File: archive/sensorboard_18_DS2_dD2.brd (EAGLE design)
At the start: 100 x 58 mm, 91 parts, among them IC1 ECMF02-2AMX6, IC2_ESP32S2WROOMM22S2 ESP32-S2-WROOM_M22S2H3200PH3Q0, J1_CONN._ADAPTERB. RJ12, J4_USB USB_CONN, J6_OAT 2.5mm JACK, J7_I2C RJ12, U1 LPS22HB, U10-MAG_SENSOR MMC5983MA, U11 LDL212PV33R, U12 NCV8163ASN330T1G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

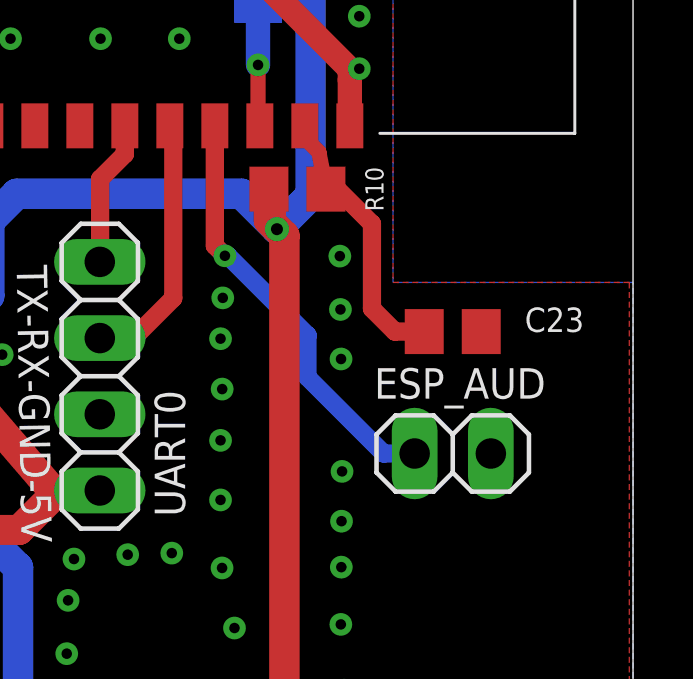
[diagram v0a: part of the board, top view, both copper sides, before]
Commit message: Archive v18 files
Create archive directory with v18 files for use as assembly reference for previous board revision
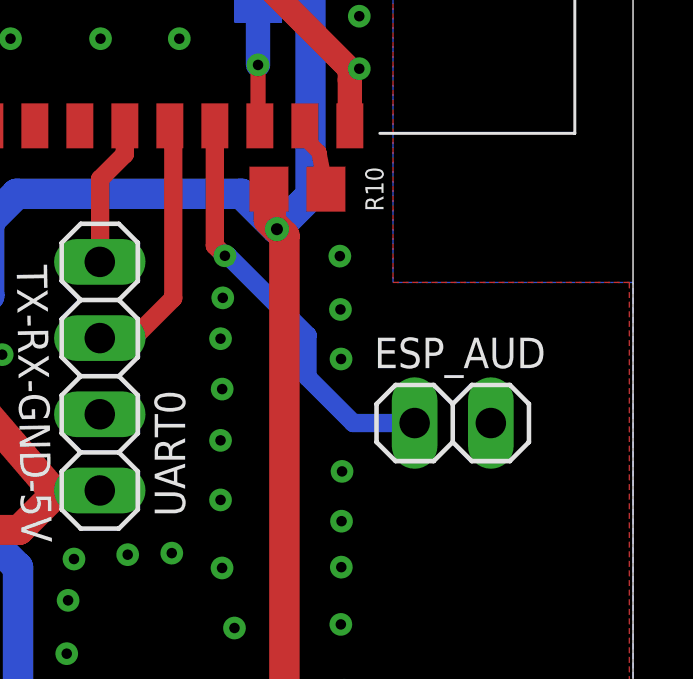
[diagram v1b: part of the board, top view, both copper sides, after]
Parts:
- removed C23: 100nF, rcl:C0805
- moved ESP_AUD 1.02 mm to (99.3, 42.4)
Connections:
- net GND: no longer C23.2
- net N$7: no longer C23.1
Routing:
- net N$7: track 9.23 -> 2.33 mm
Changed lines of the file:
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@@
 <attribute name="VALUE" x="98.2546" y="21.9201" size="1.27" layer="27" rot="R90" align="center"/>
 </element>
-<element name="ESP_AUD" library="pinhead" library_urn="urn:adsk.eagle:library:325" package="1X02" package3d_urn="urn:adsk.eagle:package:22435/2" value="" x="99.2759" y="41.3766" smashed="yes">
-<attribute name="NAME" x="96.6597" y="43.2054" size="1.016" layer="25" ratio="10"/>
-<attribute name="POPULARITY" value="98" x="99.2759" y="41.3766" size="1.778" layer="27" display="off"/>
-<attribute name="VALUE" x="96.7359" y="38.2016" size="1.27" layer="27"/>
-</element>
-<element name="C23" library="rcl" library_urn="urn:adsk.eagle:library:334" package="C0805" package3d_urn="urn:adsk.eagle:package:23617/2" value="100nF" x="99.2759" y="45.4406" smashed="yes">
-<attribute name="NAME" x="101.6762" y="45.4279" size="0.8128" layer="25"/>
-<attribute name="POPULARITY" value="88" x="99.2759" y="45.4406" size="1.778" layer="27" display="off"/>
-<attribute name="SPICEPREFIX" value="C" x="99.2759" y="45.4406" size="1.778" layer="27" display="off"/>
-<attribute name="VALUE" x="98.0059" y="42.9006" size="1.27" layer="27"/>
+<element name="ESP_AUD" library="pinhead" library_urn="urn:adsk.eagle:library:325" package="1X02" package3d_urn="urn:adsk.eagle:package:22435/2" value="" x="99.2759" y="42.3926" smashed="yes">
+<attribute name="NAME" x="96.6597" y="44.2214" size="1.016" layer="25" ratio="10"/>
+<attribute name="POPULARITY" value="98" x="99.2759" y="42.3926" size="1.778" layer="27" display="off"/>
+<attribute name="VALUE" x="96.7359" y="39.2176" size="1.27" layer="27"/>
 </element>
 </elements>
@@
 <via x="57.6332" y="59.9216" extent="1-16" drill="0.35"/>
 <contactref element="ESP_AUD" pad="2"/>
-<contactref element="C23" pad="2"/>
 </signal>
 <signal name="VDD1">
@@
 <wire x1="94.812503125" y1="51.427196875" x2="95.0506" y2="50.1891" width="0.508" layer="1"/>
 <wire x1="94.3456" y1="51.8941" x2="94.812503125" y2="51.427196875" width="0.508" layer="1"/>
-<contactref element="C23" pad="1"/>
-<wire x1="98.3259" y1="45.4406" x2="97.348" y2="45.4406" width="0.6096" layer="1"/>
-<wire x1="97.348" y1="45.4406" x2="96.5835" y2="46.2051" width="0.6096" layer="1"/>
-<wire x1="96.5835" y1="46.2051" x2="96.5835" y2="49.0347" width="0.6096" layer="1"/>
-<wire x1="96.5835" y1="49.0347" x2="95.4291" y2="50.1891" width="0.6096" layer="1"/>
-<wire x1="95.4291" y1="50.1891" x2="95.0506" y2="50.1891" width="0.6096" layer="1"/>
 </signal>
 <signal name="N$9">
@@
 <wire x1="94.4372" y1="45.3136" x2="91.7829" y2="47.9679" width="0.6096" layer="16"/>
 <wire x1="94.4372" y1="45.3136" x2="94.4372" y2="43.9166" width="0.6096" layer="16"/>
-<wire x1="94.4372" y1="43.9166" x2="96.9772" y2="41.3766" width="0.6096" layer="16"/>
-<wire x1="96.9772" y1="41.3766" x2="98.0059" y2="41.3766" width="0.6096" layer="16"/>
+<wire x1="94.4372" y1="43.9166" x2="95.9612" y2="42.3926" width="0.6096" layer="16"/>
+<wire x1="95.9612" y1="42.3926" x2="98.0059" y2="42.3926" width="0.6096" layer="16"/>
 </signal>
 <signal name="5V_EXT">
